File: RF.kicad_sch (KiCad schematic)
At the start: 53 parts, among them J1 Conn_Coaxial_Small, J5 2.4Ghz Antenna, U4 LR1121IMLTRT, U8 SKY13588-460LF, Y3 32.768KHz, Y4 32MHz

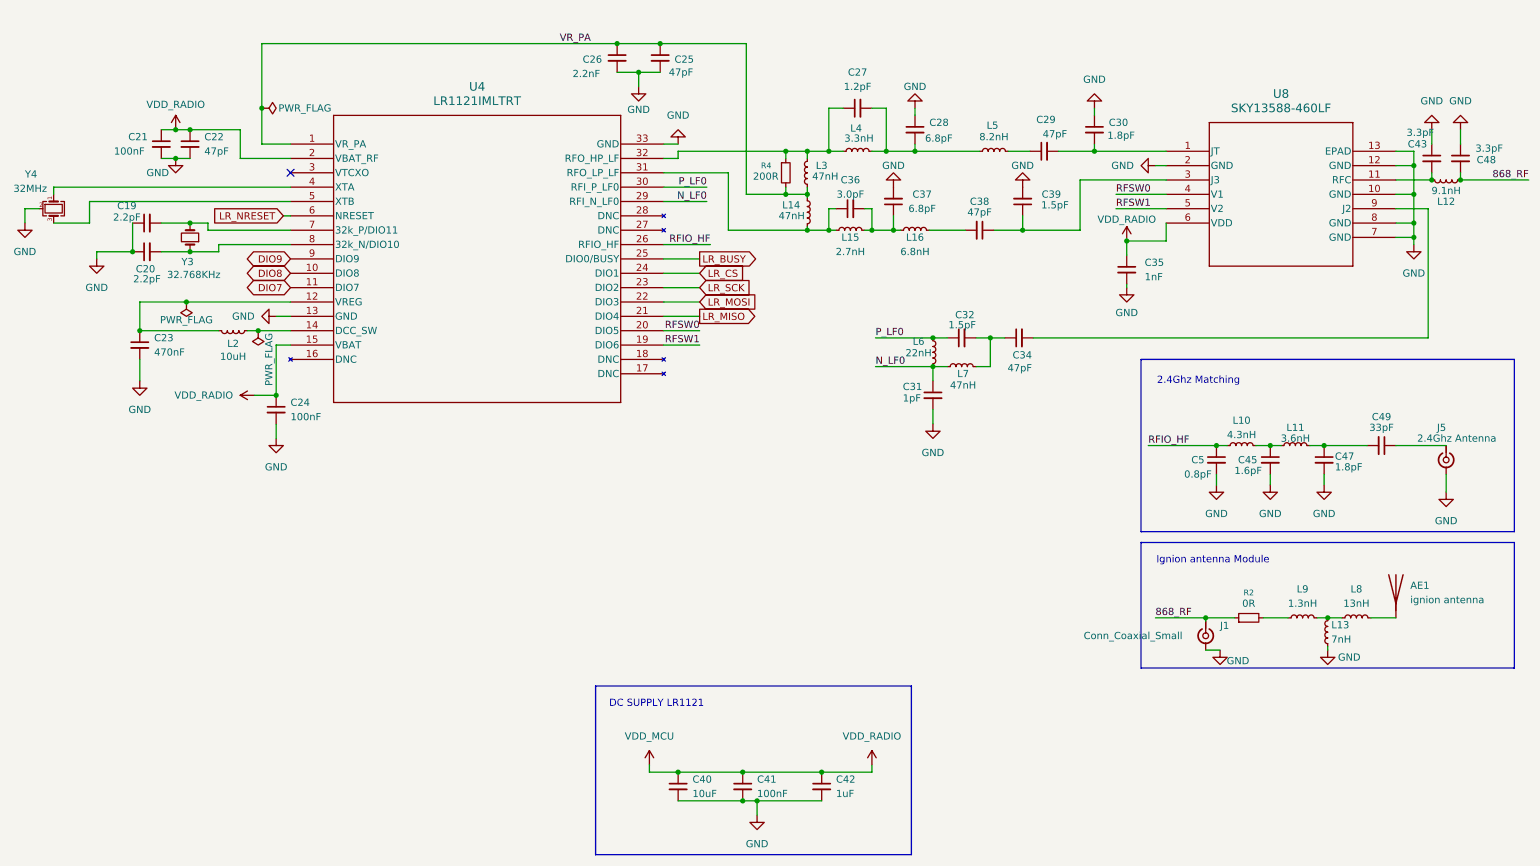
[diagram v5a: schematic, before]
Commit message: fix smtp line and minor errors
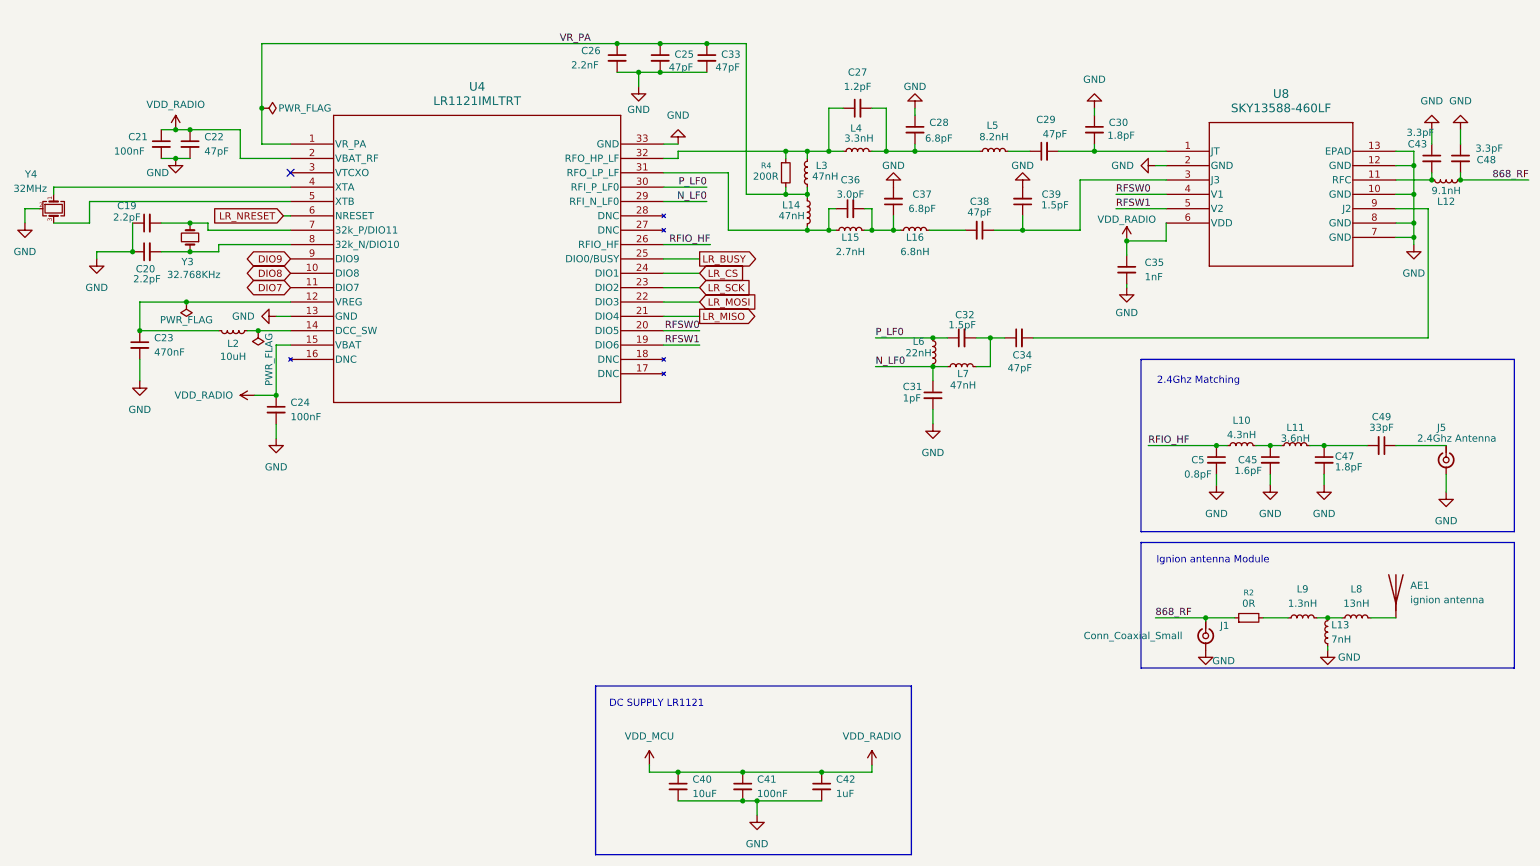
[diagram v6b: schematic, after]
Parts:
- added C33: 47pF, Capacitor_SMD:C_0201_0603Metric, symbol Device:C_Small
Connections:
- net GND: now also C33.2
- net VR_PA: now also C33.1
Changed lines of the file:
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@@
 	)
 	(junction
+		(at 138.43 52.07)
+		(diameter 0)
+		(color 0 0 0 0)
+	)
+	(junction
 		(at 59.055 102.87)
 		(diameter 0)
@@
 	)
 	(junction
+		(at 130.175 57.15)
+		(diameter 0)
+		(color 0 0 0 0)
+	)
+	(junction
 		(at 212.725 86.995)
 		(diameter 0)
@@
 	(wire
 		(pts
+			(xy 130.175 57.15) (xy 138.43 57.15)
+		)
+		(stroke
+			(width 0)
+			(type default)
+		)
+	)
+	(wire
+		(pts
 			(xy 44.45 72.39) (xy 46.99 72.39)
 		)
@@
 	(wire
 		(pts
+			(xy 138.43 52.07) (xy 145.415 52.07)
+		)
+		(stroke
+			(width 0)
+			(type default)
+		)
+	)
+	(wire
+		(pts
 			(xy 238.125 123.19) (xy 240.03 123.19)
 		)
@@
 	(wire
 		(pts
-			(xy 145.415 52.07) (xy 130.175 52.07)
-		)
-		(stroke
-			(width 0)
-			(type default)
-		)
-	)
-	(wire
-		(pts
 			(xy 207.01 71.12) (xy 219.71 71.12)
 		)
@@
 	(wire
 		(pts
-			(xy 226.695 159.385) (xy 229.235 159.385)
-		)
-		(stroke
-			(width 0)
-			(type default)
-		)
-	)
-	(wire
-		(pts
 			(xy 188.595 109.22) (xy 186.055 109.22)
 		)
@@
 	(wire
 		(pts
+			(xy 130.175 52.07) (xy 138.43 52.07)
+		)
+		(stroke
+			(width 0)
+			(type default)
+		)
+	)
+	(wire
+		(pts
 			(xy 142.24 85.09) (xy 156.21 85.09)
 		)
@@
 	)
 	(symbol
+		(lib_id "Device:C_Small")
+		(at 138.43 54.61 0)
+		(unit 1)
+		(exclude_from_sim no)
+		(in_bom yes)
+		(on_board yes)
+		(dnp no)
+		(property "Reference" "C33"
+			(at 140.97 53.975 0)
+			(effects
+				(font
+					(size 1.27 1.27)
+				)
+				(justify left)
+			)
+		)
+		(property "Value" "47pF"
+			(at 139.954 56.261 0)
+			(effects
+				(font
+					(size 1.27 1.27)
+				)
+				(justify left)
+			)
+		)
+		(property "Footprint" "Capacitor_SMD:C_0201_0603Metric"
+			(at 138.43 54.61 0)
+			(effects
+				(font
+					(size 1.27 1.27)
+				)
+				(hide yes)
+			)
+		)
+		(property "Datasheet" "~"
+			(at 138.43 54.61 0)
+			(effects
+				(font
+					(size 1.27 1.27)
+				)
+				(hide yes)
+			)
+		)
+		(property "Description" "Unpolarized capacitor, small symbol"
+			(at 138.43 54.61 0)
+			(effects
+				(font
+					(size 1.27 1.27)
+				)
+				(hide yes)
+			)
+		)
+		(pin "2"
+		)
+		(pin "1"
+		)
+		(instances
+			(project "lora-stmu535-lr1121-tx"
+				(path "/963238c7-8564-44c5-a128-5d82375c10f7/5e252930-8cb6-4106-8539-d7be2478662a"
+					(reference "C33")
+					(unit 1)
+				)
+			)
+		)
+	)
+	(symbol
 		(lib_id "power:GND")
 		(at 44.45 72.39 0)
@@
 		(dnp no)
 		(property "Reference" "C25"
-			(at 132.715 54.864 0)
+			(at 132.715 53.975 0)
 			(effects
 				(font
@@
 		)
 		(property "Value" "47pF"
-			(at 131.699 57.15 0)
+			(at 131.699 56.261 0)
 			(effects
 				(font
@@
 	(symbol
 		(lib_id "power:GND")
-		(at 229.235 159.385 0)
+		(at 226.695 159.385 0)
 		(unit 1)
 		(exclude_from_sim no)
@@
 		(dnp no)
 		(property "Reference" "#PWR030"
-			(at 229.235 165.735 0)
+			(at 226.695 165.735 0)
 			(effects
 				(font
@@
 		)
 		(property "Value" "GND"
-			(at 232.41 161.29 0)
+			(at 229.87 161.29 0)
 			(effects
 				(font
@@
 		)
 		(property "Footprint" ""
-			(at 229.235 159.385 0)
+			(at 226.695 159.385 0)
 			(effects
 				(font
@@
 		)
 		(property "Datasheet" ""
-			(at 229.235 159.385 0)
+			(at 226.695 159.385 0)
 			(effects
 				(font
@@
 		)
 		(property "Description" "Power symbol creates a global label with name \"GND\" , ground"
-			(at 229.235 159.385 0)
+			(at 226.695 159.385 0)
 			(effects
 				(font
@@
 		(dnp no)
 		(property "Reference" "C26"
-			(at 116.459 54.864 0)
+			(at 116.205 53.34 0)
 			(effects
 				(font
@@
 		)
 		(property "Value" "2.2nF"
-			(at 114.681 57.404 0)
+			(at 114.427 55.88 0)
 			(effects
 				(font
